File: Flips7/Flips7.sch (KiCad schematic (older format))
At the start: 11 parts, among them U1 FP2800A, U2 FP2800A, U3 FP2800A

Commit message: adding row driver share connectors
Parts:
- added CN1, CN2: Conn_02x16_Odd_Even, Pin_Headers:Pin_Header_Straight_2x16_Pitch2.54mm, symbol Connector_Generic:Conn_02x16_Odd_Even
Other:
- moved on the sheet: BOARD1

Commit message: rename row pins to /SY## and RY##
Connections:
- net labels added: RY01, RY02, RY03, RY04, RY05, RY06, RY07, RY08, RY09, RY10, RY11, RY12, RY13, RY14, RY15, RY16, ~SY01, ~SY02, ~SY03, ~SY04, ~SY05, ~SY06, ~SY07, ~SY08, ~SY09, ~SY10, ~SY11, ~SY12, ~SY13, ~SY14, ~SY15, ~SY16
- net labels removed: YR01, YR02, YR03, YR04, YR05, YR06, YR07, YR08, YR09, YR10, YR11, YR12, YR13, YR14, YR15, YR16, YS01, YS02, YS03, YS04, YS05, YS06, YS07, YS08, YS09, YS10, YS11, YS12, YS13, YS14, YS15, YS16

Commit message: new routing attempt (wip) for Flips7
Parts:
- removed CN1, CN2: Conn_02x16_Odd_Even, Pin_Headers:Pin_Header_Straight_2x16_Pitch2.54mm, symbol Connector_Generic:Conn_02x16_Odd_Even
- added CN1, CN2: Conn_02x17_Odd_Even, Own:Pin_Header_Straight_Shrouded_2x17_Pitch2.54mm_ConvNumbering, symbol Connector_Generic:Conn_02x17_Odd_Even
- BOARD1: footprint IDC_Numbering_Pin_Header_Straight_2x30_Pitch2.54mm -> Own:Pin_Header_Straight_Shrouded_2x30_Pitch2.54mm_AltNumbering
- CNX1, CNY1, CNY2: footprint Own:Pin_Header_Angle_Shrouded_2x05_Pitch2.54mm -> Own:Pin_Header_Angle_Shrouded_2x05_Pitch2.54mm_ConvNumbering
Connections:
- no-connect marks 27 -> 31
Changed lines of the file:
@@
 F 0 "CNY1" H 5150 1517 50  0000 C CNN
 F 1 "UFP2810" H 5150 1426 50  0000 C CNN
-F 2 "Own:Pin_Header_Angle_Shrouded_2x05_Pitch2.54mm" H 5150 1050 50  0001 C CNN
+F 2 "Own:Pin_Header_Angle_Shrouded_2x05_Pitch2.54mm_ConvNumbering" H 5150 1050 50  0001 C CNN
 F 3 "" H 5150 1050 50  0001 C CNN
 	1    5150 1050
@@
 F 0 "CNY2" H 8200 1517 50  0000 C CNN
 F 1 "UFP2810" H 8200 1426 50  0000 C CNN
-F 2 "Own:Pin_Header_Angle_Shrouded_2x05_Pitch2.54mm" H 8200 1050 50  0001 C CNN
+F 2 "Own:Pin_Header_Angle_Shrouded_2x05_Pitch2.54mm_ConvNumbering" H 8200 1050 50  0001 C CNN
 F 3 "" H 8200 1050 50  0001 C CNN
 	1    8200 1050
@@
 F 0 "CNX1" H 2250 5667 50  0000 C CNN
 F 1 "UFP2810" H 2250 5576 50  0000 C CNN
-F 2 "Own:Pin_Header_Angle_Shrouded_2x05_Pitch2.54mm" H 2250 5200 50  0001 C CNN
+F 2 "Own:Pin_Header_Angle_Shrouded_2x05_Pitch2.54mm_ConvNumbering" H 2250 5200 50  0001 C CNN
 F 3 "" H 2250 5200 50  0001 C CNN
 	1    2250 5200
@@
 F 0 "BOARD1" H 6050 5817 50  0000 C CNN
 F 1 "Conn_02x30_Top_Bottom" H 6050 5726 50  0000 C CNN
-F 2 "IDC_Numbering_Pin_Header_Straight_2x30_Pitch2.54mm" H 6000 4200 50  0001 C CNN
+F 2 "Own:Pin_Header_Straight_Shrouded_2x30_Pitch2.54mm_AltNumbering" H 6000 4200 50  0001 C CNN
 F 3 "~" H 6000 4200 50  0001 C CNN
 	1    6000 4200
@@
 Text Label 8300 4400 2    50   ~ 0
 ~SY04
+Text Label 8300 4600 2    50   ~ 0
+~SY05
 Text Label 8300 4500 2    50   ~ 0
-~SY05
-Text Label 8300 4600 2    50   ~ 0
 ~SY06
 Text Label 8300 4700 2    50   ~ 0
 ~SY07
+Text Label 8300 5100 2    50   ~ 0
+~SY08
+Text Label 8300 5200 2    50   ~ 0
+~SY09
+Text Label 8300 5300 2    50   ~ 0
+~SY10
+Text Label 8300 5500 2    50   ~ 0
+~SY11
+Text Label 8300 4900 2    50   ~ 0
+~SY12
+Text Label 8300 5400 2    50   ~ 0
+~SY13
 Text Label 8300 4800 2    50   ~ 0
-~SY08
-Text Label 8300 4900 2    50   ~ 0
-~SY09
-Text Label 8300 5000 2    50   ~ 0
-~SY10
-Text Label 8300 5100 2    50   ~ 0
-~SY11
-Text Label 8300 5200 2    50   ~ 0
-~SY12
-Text Label 8300 5300 2    50   ~ 0
-~SY13
-Text Label 8300 5400 2    50   ~ 0
 ~SY14
-Text Label 8800 4100 0    50   ~ 0
+Text Label 10000 5100 0    50   ~ 0
 RY01
-Text Label 8800 4200 0    50   ~ 0
+Text Label 10000 5200 0    50   ~ 0
 RY02
-Text Label 8800 4300 0    50   ~ 0
+Text Label 10000 5300 0    50   ~ 0
 RY03
-Text Label 8800 4400 0    50   ~ 0
+Text Label 8800 5500 0    50   ~ 0
 RY04
-Text Label 8800 4500 0    50   ~ 0
+Text Label 8800 4900 0    50   ~ 0
 RY05
+Text Label 8800 5400 0    50   ~ 0
+RY06
+Text Label 10000 4800 0    50   ~ 0
+RY07
+Text Label 10000 4100 0    50   ~ 0
+RY08
+Text Label 10000 4200 0    50   ~ 0
+RY09
+Text Label 10000 4300 0    50   ~ 0
+RY10
+Text Label 10000 4400 0    50   ~ 0
+RY11
 Text Label 8800 4600 0    50   ~ 0
-RY06
-Text Label 8800 4700 0    50   ~ 0
-RY07
-Text Label 8800 4800 0    50   ~ 0
-RY08
-Text Label 8800 4900 0    50   ~ 0
-RY09
-Text Label 8800 5000 0    50   ~ 0
-RY10
-Text Label 8800 5100 0    50   ~ 0
-RY11
-Text Label 8800 5200 0    50   ~ 0
 RY12
-Text Label 8800 5300 0    50   ~ 0
+Text Label 10000 4500 0    50   ~ 0
 RY13
-Text Label 8800 5400 0    50   ~ 0
+Text Label 10000 4700 0    50   ~ 0
 RY14
-Text Label 8300 5500 2    50   ~ 0
+Text Label 8300 5600 2    50   ~ 0
 ~SY15
-Text Label 8300 5600 2    50   ~ 0
+Text Label 8300 5700 2    50   ~ 0
 ~SY16
-Text Label 8800 5500 0    50   ~ 0
+Text Label 10000 5600 0    50   ~ 0
 RY15
-Text Label 8800 5600 0    50   ~ 0
+Text Label 10000 5700 0    50   ~ 0
 RY16
 Text Label 9500 4100 2    50   ~ 0
@@
 Text Label 9500 4400 2    50   ~ 0
 ~SY04
+Text Label 9500 4600 2    50   ~ 0
+~SY05
 Text Label 9500 4500 2    50   ~ 0
-~SY05
-Text Label 9500 4600 2    50   ~ 0
 ~SY06
 Text Label 9500 4700 2    50   ~ 0
 ~SY07
+Text Label 9500 5100 2    50   ~ 0
+~SY08
+Text Label 9500 5200 2    50   ~ 0
+~SY09
+Text Label 9500 5300 2    50   ~ 0
+~SY10
+Text Label 9500 5500 2    50   ~ 0
+~SY11
+Text Label 9500 4900 2    50   ~ 0
+~SY12
+Text Label 9500 5400 2    50   ~ 0
+~SY13
 Text Label 9500 4800 2    50   ~ 0
-~SY08
-Text Label 9500 4900 2    50   ~ 0
-~SY09
-Text Label 9500 5000 2    50   ~ 0
-~SY10
-Text Label 9500 5100 2    50   ~ 0
-~SY11
-Text Label 9500 5200 2    50   ~ 0
-~SY12
-Text Label 9500 5300 2    50   ~ 0
-~SY13
-Text Label 9500 5400 2    50   ~ 0
 ~SY14
-Text Label 10000 4100 0    50   ~ 0
+Text Label 8800 5100 0    50   ~ 0
 RY01
-Text Label 10000 4200 0    50   ~ 0
+Text Label 8800 5200 0    50   ~ 0
 RY02
-Text Label 10000 4300 0    50   ~ 0
+Text Label 8800 5300 0    50   ~ 0
 RY03
-Text Label 10000 4400 0    50   ~ 0
+Text Label 10000 5500 0    50   ~ 0
 RY04
-Text Label 10000 4500 0    50   ~ 0
+Text Label 10000 4900 0    50   ~ 0
 RY05
+Text Label 10000 5400 0    50   ~ 0
+RY06
+Text Label 8800 4800 0    50   ~ 0
+RY07
+Text Label 8800 4100 0    50   ~ 0
+RY08
+Text Label 8800 4200 0    50   ~ 0
+RY09
+Text Label 8800 4300 0    50   ~ 0
+RY10
+Text Label 8800 4400 0    50   ~ 0
+RY11
 Text Label 10000 4600 0    50   ~ 0
-RY06
-Text Label 10000 4700 0    50   ~ 0
-RY07
-Text Label 10000 4800 0    50   ~ 0
-RY08
-Text Label 10000 4900 0    50   ~ 0
-RY09
-Text Label 10000 5000 0    50   ~ 0
-RY10
-Text Label 10000 5100 0    50   ~ 0
-RY11
-Text Label 10000 5200 0    50   ~ 0
 RY12
-Text Label 10000 5300 0    50   ~ 0
+Text Label 8800 4500 0    50   ~ 0
 RY13
-Text Label 10000 5400 0    50   ~ 0
+Text Label 8800 4700 0    50   ~ 0
 RY14
-Text Label 9500 5500 2    50   ~ 0
+Text Label 9500 5600 2    50   ~ 0
 ~SY15
-Text Label 9500 5600 2    50   ~ 0
+Text Label 9500 5700 2    50   ~ 0
 ~SY16
-Text Label 10000 5500 0    50   ~ 0
+Text Label 8800 5600 0    50   ~ 0
 RY15
-Text Label 10000 5600 0    50   ~ 0
+Text Label 8800 5700 0    50   ~ 0
 RY16
 $Comp
-L Connector_Generic:Conn_02x16_Odd_Even CN1
-U 1 1 5BE0CD77
-P 8500 4800
-F 0 "CN1" H 8550 5717 50  0000 C CNN
-F 1 "Conn_02x16_Odd_Even" H 8550 5626 50  0000 C CNN
-F 2 "Pin_Headers:Pin_Header_Straight_2x16_Pitch2.54mm" H 8500 4800 50  0001 C CNN
-F 3 "~" H 8500 4800 50  0001 C CNN
-	1    8500 4800
+L Connector_Generic:Conn_02x17_Odd_Even CN1
+U 1 1 5BEB5E2C
+P 8500 4900
+F 0 "CN1" H 8550 5917 50  0000 C CNN
+F 1 "Conn_02x17_Odd_Even" H 8550 5826 50  0000 C CNN
+F 2 "Own:Pin_Header_Straight_Shrouded_2x17_Pitch2.54mm_ConvNumbering" H 8500 4900 50  0001 C CNN
+F 3 "~" H 8500 4900 50  0001 C CNN
+	1    8500 4900
 	1    0    0    -1
 $EndComp
 $Comp
-L Connector_Generic:Conn_02x16_Odd_Even CN2
-U 1 1 5BE0CDEE
-P 9700 4800
-F 0 "CN2" H 9750 5717 50  0000 C CNN
-F 1 "Conn_02x16_Odd_Even" H 9750 5626 50  0000 C CNN
-F 2 "Pin_Headers:Pin_Header_Straight_2x16_Pitch2.54mm" H 9700 4800 50  0001 C CNN
-F 3 "~" H 9700 4800 50  0001 C CNN
-	1    9700 4800
+L Connector_Generic:Conn_02x17_Odd_Even CN2
+U 1 1 5BEB679A
+P 9700 4900
+F 0 "CN2" H 9750 5917 50  0000 C CNN
+F 1 "Conn_02x17_Odd_Even" H 9750 5826 50  0000 C CNN
+F 2 "Own:Pin_Header_Straight_Shrouded_2x17_Pitch2.54mm_ConvNumbering" H 9700 4900 50  0001 C CNN
+F 3 "~" H 9700 4900 50  0001 C CNN
+	1    9700 4900
 	1    0    0    -1
 $EndComp
+NoConn ~ 8300 5000
+NoConn ~ 8800 5000
+NoConn ~ 9500 5000
+NoConn ~ 10000 5000
 $EndSCHEMATC

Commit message: single GND, VCC and HV; almost finish tracing
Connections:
- net labels added: GND, HV, VCC
- net labels removed: L.GND, L.HV, L.VCC, R.GND, R.HV, R.VCC, X.GND, X.HV, X.VCC
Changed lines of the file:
@@
 L.EN
 Text Label 4800 1050 2    50   ~ 0
-L.HV
+HV
 Text Label 4800 1150 2    50   ~ 0
-L.VCC
+VCC
 Text Label 4800 1250 2    50   ~ 0
 L.A0
@@
 L.POL
 Text Label 5500 1050 0    50   ~ 0
-L.GND
+GND
 Text Label 5500 1150 0    50   ~ 0
 L.A1
@@
 R.A0
 Text Label 600  2000 1    50   ~ 0
-L.GND
+GND
 Text Label 600  2450 1    50   ~ 0
-L.GND
+GND
 Text Label 4600 1950 0    50   ~ 0
-L.VCC
+VCC
 Text Label 4600 2350 0    50   ~ 0
-L.HV
+HV
 Text Label 8550 850  0    50   ~ 0
 R.B0
@@
 R.POL
 Text Label 8550 1050 0    50   ~ 0
-R.GND
+GND
 Text Label 8550 1150 0    50   ~ 0
 R.A1
@@
 R.EN
 Text Label 7850 1050 2    50   ~ 0
-R.HV
+HV
 Text Label 7850 1150 2    50   ~ 0
-R.VCC
+VCC
 Text Label 7850 1250 2    50   ~ 0
 R.A0
 Text Label 6750 2100 2    50   ~ 0
-R.GND
+GND
 Text Label 6750 2550 2    50   ~ 0
-R.GND
+GND
 Text Label 10750 2450 0    50   ~ 0
-R.HV
+HV
 Text Label 10750 2050 0    50   ~ 0
-R.VCC
+VCC
 $Comp
 L power:PWR_FLAG #FLG0101
@@
 	0    -1   -1   0
 $EndComp
-$Comp
-L power:PWR_FLAG #FLG0104
-U 1 1 5BDFAC70
-P 2450 750
-F 0 "#FLG0104" H 2450 825 50  0001 C CNN
-F 1 "PWR_FLAG" V 2450 878 50  0000 L CNN
-F 2 "" H 2450 750 50  0001 C CNN
-F 3 "~" H 2450 750 50  0001 C CNN
-	1    2450 750
-	0    -1   -1   0
-$EndComp
-$Comp
-L power:PWR_FLAG #FLG0105
-U 1 1 5BDFAC85
-P 2450 850
-F 0 "#FLG0105" H 2450 925 50  0001 C CNN
-F 1 "PWR_FLAG" V 2450 978 50  0000 L CNN
-F 2 "" H 2450 850 50  0001 C CNN
-F 3 "~" H 2450 850 50  0001 C CNN
-	1    2450 850
-	0    -1   -1   0
-$EndComp
-$Comp
-L power:PWR_FLAG #FLG0106
-U 1 1 5BDFAC9A
-P 2450 950
-F 0 "#FLG0106" H 2450 1025 50  0001 C CNN
-F 1 "PWR_FLAG" V 2450 1078 50  0000 L CNN
-F 2 "" H 2450 950 50  0001 C CNN
-F 3 "~" H 2450 950 50  0001 C CNN
-	1    2450 950
-	0    -1   -1   0
-$EndComp
 Text Label 1500 750  0    50   ~ 0
-L.GND
+GND
 Text Label 1500 850  0    50   ~ 0
-L.VCC
+VCC
 Text Label 1500 950  0    50   ~ 0
-L.HV
-Text Label 2450 750  0    50   ~ 0
-R.GND
-Text Label 2450 850  0    50   ~ 0
-R.VCC
-Text Label 2450 950  0    50   ~ 0
-R.HV
+HV
 $Comp
 L Device:C_Small C1
@@
 	4600 1600 4600 1650
 Text Label 4600 1600 0    50   ~ 0
-L.GND
+GND
 Text Label 10750 1700 0    50   ~ 0
-R.GND
+GND
 Text Label 4050 3050 3    50   ~ 0
 ~SY01
@@
 X.POL
 Text Label 2600 5200 0    50   ~ 0
-X.GND
+GND
 Text Label 2600 5300 0    50   ~ 0
 X.A1
@@
 X.EN
 Text Label 1900 5200 2    50   ~ 0
-X.HV
+HV
 Text Label 1900 5300 2    50   ~ 0
-X.VCC
+VCC
 Text Label 1900 5400 2    50   ~ 0
 X.A0
 Text Label 800  6250 2    50   ~ 0
-X.GND
+GND
 Text Label 800  6700 2    50   ~ 0
-X.GND
+GND
 Text Label 4800 6600 0    50   ~ 0
-X.HV
+HV
 Text Label 4800 6200 0    50   ~ 0
-X.VCC
+VCC
 $Comp
 L Device:C_Small C3
@@
 	4800 6100 4800 6200
 Text Label 4800 5850 0    50   ~ 0
-X.GND
+GND
 Text Label 4250 7300 3    50   ~ 0
 X01
@@
 NoConn ~ 4450 7300
 $Comp
-L power:PWR_FLAG #FLG01
-U 1 1 5BE4CDC2
-P 3400 750
-F 0 "#FLG01" H 3400 825 50  0001 C CNN
-F 1 "PWR_FLAG" V 3400 878 50  0000 L CNN
-F 2 "" H 3400 750 50  0001 C CNN
-F 3 "~" H 3400 750 50  0001 C CNN
-	1    3400 750
-	0    -1   -1   0
-$EndComp
-$Comp
-L power:PWR_FLAG #FLG02
-U 1 1 5BE4CDC8
-P 3400 850
-F 0 "#FLG02" H 3400 925 50  0001 C CNN
-F 1 "PWR_FLAG" V 3400 978 50  0000 L CNN
-F 2 "" H 3400 850 50  0001 C CNN
-F 3 "~" H 3400 850 50  0001 C CNN
-	1    3400 850
-	0    -1   -1   0
-$EndComp
-$Comp
-L power:PWR_FLAG #FLG03
-U 1 1 5BE4CDCE
-P 3400 950
-F 0 "#FLG03" H 3400 1025 50  0001 C CNN
-F 1 "PWR_FLAG" V 3400 1078 50  0000 L CNN
-F 2 "" H 3400 950 50  0001 C CNN
-F 3 "~" H 3400 950 50  0001 C CNN
-	1    3400 950
-	0    -1   -1   0
-$EndComp
-Text Label 3400 750  0    50   ~ 0
-X.GND
-Text Label 3400 850  0    50   ~ 0
-X.VCC
-Text Label 3400 950  0    50   ~ 0
-X.HV
-$Comp
 L Connector_Generic:Conn_02x30_Top_Bottom BOARD1

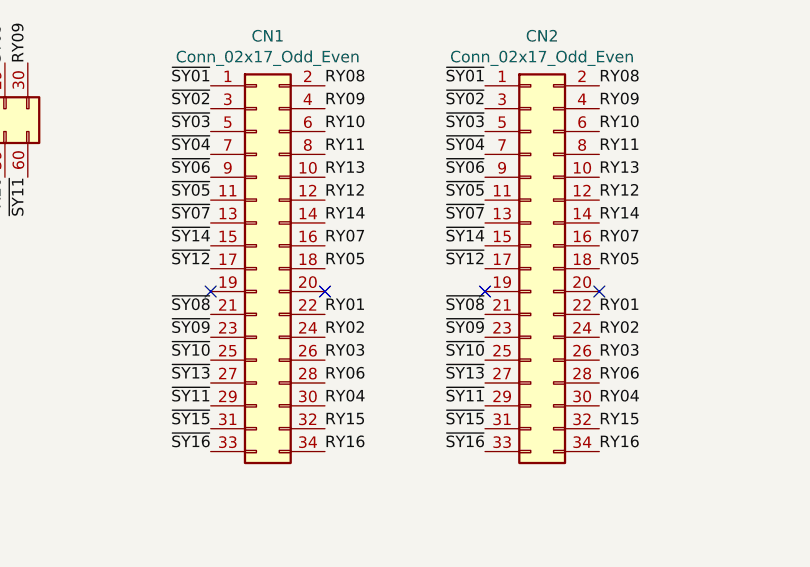
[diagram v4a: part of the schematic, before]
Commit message: GND on share connectors
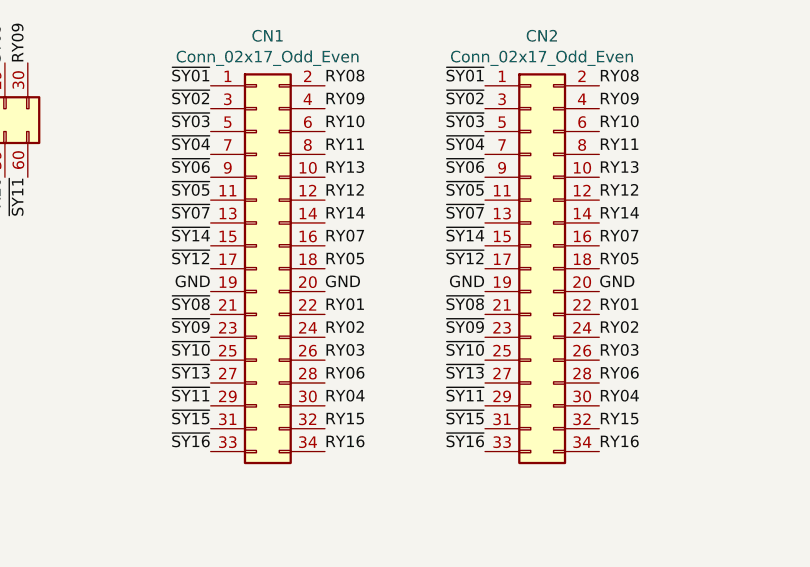
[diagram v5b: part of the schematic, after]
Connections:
- no-connect marks 31 -> 27
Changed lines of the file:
@@
 	1    0    0    -1
 $EndComp
-NoConn ~ 8300 5000
-NoConn ~ 8800 5000
-NoConn ~ 9500 5000
-NoConn ~ 10000 5000
+Text Label 8300 5000 2    50   ~ 0
+GND
+Text Label 9500 5000 2    50   ~ 0
+GND
+Text Label 8800 5000 0    50   ~ 0
+GND
+Text Label 10000 5000 0    50   ~ 0
+GND
 $EndSCHEMATC

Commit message: Fixing C values to 0µ1; connecting VCC of 3 units
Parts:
- C1, C2, C3: value 0U1 -> 0µ1
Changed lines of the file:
@@
 P 4600 1750
 F 0 "C1" H 4692 1796 50  0000 L CNN
-F 1 "0U1" H 4692 1705 50  0000 L CNN
+F 1 "0µ1" H 4692 1705 50  0000 L CNN
 F 2 "Capacitors_SMD:C_0805_HandSoldering" H 4600 1750 50  0001 C CNN
 F 3 "~" H 4600 1750 50  0001 C CNN
@@
 P 10750 1850
 F 0 "C2" H 10658 1804 50  0000 R CNN
-F 1 "0U1" H 10658 1895 50  0000 R CNN
+F 1 "0µ1" H 10658 1895 50  0000 R CNN
 F 2 "Capacitors_SMD:C_0805_HandSoldering" H 10750 1850 50  0001 C CNN
 F 3 "~" H 10750 1850 50  0001 C CNN
@@
 P 4800 6000
 F 0 "C3" H 4708 5954 50  0000 R CNN
-F 1 "0U1" H 4708 6045 50  0000 R CNN
+F 1 "0µ1" H 4708 6045 50  0000 R CNN
 F 2 "Capacitors_SMD:C_0805_HandSoldering" H 4800 6000 50  0001 C CNN
 F 3 "~" H 4800 6000 50  0001 C CNN

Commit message: adding pull downs for ENABLE pins
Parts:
- added R1, R2, R3: 10k, Resistors_SMD:R_0805_HandSoldering, symbol Device:R_Small
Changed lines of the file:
@@
 Text Label 10000 5000 0    50   ~ 0
 GND
+$Comp
+L Device:R_Small R3
+U 1 1 5BEF1C78
+P 1350 4150
+F 0 "R3" H 1409 4196 50  0000 L CNN
+F 1 "10k" H 1409 4105 50  0000 L CNN
+F 2 "Resistors_SMD:R_0805_HandSoldering" H 1350 4150 50  0001 C CNN
+F 3 "~" H 1350 4150 50  0001 C CNN
+	1    1350 4150
+	1    0    0    -1
+$EndComp
+$Comp
+L power:GND #PWR0101
+U 1 1 5BEF1DC6
+P 1350 4250
+F 0 "#PWR0101" H 1350 4000 50  0001 C CNN
+F 1 "GND" H 1355 4077 50  0000 C CNN
+F 2 "" H 1350 4250 50  0001 C CNN
+F 3 "" H 1350 4250 50  0001 C CNN
+	1    1350 4250
+	1    0    0    -1
+$EndComp
+Text Label 1350 4050 0    50   ~ 0
+X.EN
+$Comp
+L Device:R_Small R1
+U 1 1 5BEF1F26
+P 2600 1000
+F 0 "R1" H 2659 1046 50  0000 L CNN
+F 1 "10k" H 2659 955 50  0000 L CNN
+F 2 "Resistors_SMD:R_0805_HandSoldering" H 2600 1000 50  0001 C CNN
+F 3 "~" H 2600 1000 50  0001 C CNN
+	1    2600 1000
+	1    0    0    -1
+$EndComp
+$Comp
+L power:GND #PWR0102
+U 1 1 5BEF1F2D
+P 2600 1100
+F 0 "#PWR0102" H 2600 850 50  0001 C CNN
+F 1 "GND" H 2605 927 50  0000 C CNN
+F 2 "" H 2600 1100 50  0001 C CNN
+F 3 "" H 2600 1100 50  0001 C CNN
+	1    2600 1100
+	1    0    0    -1
+$EndComp
+Text Label 2600 900  0    50   ~ 0
+L.EN
+$Comp
+L Device:R_Small R2
+U 1 1 5BEF202A
+P 10450 1000
+F 0 "R2" H 10509 1046 50  0000 L CNN
+F 1 "10k" H 10509 955 50  0000 L CNN
+F 2 "Resistors_SMD:R_0805_HandSoldering" H 10450 1000 50  0001 C CNN
+F 3 "~" H 10450 1000 50  0001 C CNN
+	1    10450 1000
+	1    0    0    -1
+$EndComp
+$Comp
+L power:GND #PWR0103
+U 1 1 5BEF2031
+P 10450 1100
+F 0 "#PWR0103" H 10450 850 50  0001 C CNN
+F 1 "GND" H 10455 927 50  0000 C CNN
+F 2 "" H 10450 1100 50  0001 C CNN
+F 3 "" H 10450 1100 50  0001 C CNN
+	1    10450 1100
+	1    0    0    -1
+$EndComp
+Text Label 10450 900  0    50   ~ 0
+R.EN
 $EndSCHEMATC

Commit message: rename some symbols
rename L.## and R.## nets to Y1.## and Y2.##
rename CN1 and CN2 to SHR1 and SHR2
rename U1/2/3 to IC1/2/3
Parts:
- renumbered U1 to IC1, U2 to IC2, U3 to IC3, CN1 to SHR1, CN2 to SHR2
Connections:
- net labels added: Y1.A0, Y1.A1, Y1.A2, Y1.B0, Y1.B1, Y1.EN, Y1.POL, Y2.A0, Y2.A1, Y2.A2, Y2.B0, Y2.B1, Y2.EN, Y2.POL
- net labels removed: L.A0, L.A1, L.A2, L.B0, L.B1, L.EN, L.POL, R.A0, R.A1, R.A2, R.B0, R.B1, R.EN, R.POL
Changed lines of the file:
@@
 $EndDescr
 $Comp
-L Eigene~Bauteile:FP2800A U1
+L Eigene~Bauteile:FP2800A IC1
 U 1 1 5B82C6BE
 P 2350 2250
-F 0 "U1" V 2200 4500 60  0000 L CNN
+F 0 "IC1" V 2200 4500 60  0000 L CNN
 F 1 "FP2800A" V 2300 4500 60  0000 L CNN
 F 2 "Housings_DIP:DIP-40_W15.24mm_Socket" H 2300 2350 60  0001 C CNN
@@
 $EndComp
 $Comp
-L Eigene~Bauteile:FP2800A U2
+L Eigene~Bauteile:FP2800A IC2
 U 1 1 5B82C7AE
 P 8500 2350
-F 0 "U2" V 8350 4650 60  0000 L CNN
+F 0 "IC2" V 8350 4650 60  0000 L CNN
 F 1 "FP2800A" V 8450 4650 60  0000 L CNN
 F 2 "Housings_DIP:DIP-40_W15.24mm_Socket" H 8450 2450 60  0001 C CNN
@@
 $EndComp
 Text Label 4800 850  2    50   ~ 0
-L.B1
+Y1.B1
 Text Label 4800 950  2    50   ~ 0
-L.EN
+Y1.EN
 Text Label 4800 1050 2    50   ~ 0
 HV
@@
 VCC
 Text Label 4800 1250 2    50   ~ 0
-L.A0
+Y1.A0
 Text Label 5500 850  0    50   ~ 0
-L.B0
+Y1.B0
 Text Label 5500 950  0    50   ~ 0
-L.POL
+Y1.POL
 Text Label 5500 1050 0    50   ~ 0
 GND
 Text Label 5500 1150 0    50   ~ 0
-L.A1
+Y1.A1
 Text Label 5500 1250 0    50   ~ 0
-L.A2
+Y1.A2
 Text Label 3050 1400 1    50   ~ 0
-L.EN
+Y1.EN
 Text Label 3250 1400 1    50   ~ 0
-L.POL
+Y1.POL
 Text Label 3450 1400 1    50   ~ 0
-L.B1
+Y1.B1
 Text Label 3550 1400 1    50   ~ 0
-L.B0
+Y1.B0
 Text Label 3750 1400 1    50   ~ 0
-L.A2
+Y1.A2
 Text Label 3850 1400 1    50   ~ 0
-L.A1
+Y1.A1
 Text Label 3950 1400 1    50   ~ 0
-L.A0
+Y1.A0
 Text Label 9200 1500 1    50   ~ 0
-R.EN
+Y2.EN
 Text Label 9400 1500 1    50   ~ 0
-R.POL
+Y2.POL
 Text Label 9600 1500 1    50   ~ 0
-R.B1
+Y2.B1
 Text Label 9700 1500 1    50   ~ 0
-R.B0
+Y2.B0
 Text Label 9900 1500 1    50   ~ 0
-R.A2
+Y2.A2
 Text Label 10000 1500 1    50   ~ 0
-R.A1
+Y2.A1
 Text Label 10100 1500 1    50   ~ 0
-R.A0
+Y2.A0
 Text Label 600  2000 1    50   ~ 0
 GND
@@
 HV
 Text Label 8550 850  0    50   ~ 0
-R.B0
+Y2.B0
 Text Label 8550 950  0    50   ~ 0
-R.POL
+Y2.POL
 Text Label 8550 1050 0    50   ~ 0
 GND
 Text Label 8550 1150 0    50   ~ 0
-R.A1
+Y2.A1
 Text Label 8550 1250 0    50   ~ 0
-R.A2
+Y2.A2
 Text Label 7850 850  2    50   ~ 0
-R.B1
+Y2.B1
 Text Label 7850 950  2    50   ~ 0
-R.EN
+Y2.EN
 Text Label 7850 1050 2    50   ~ 0
 HV
@@
 VCC
 Text Label 7850 1250 2    50   ~ 0
-R.A0
+Y2.A0
 Text Label 6750 2100 2    50   ~ 0
 GND
@@
 $EndComp
 $Comp
-L Eigene~Bauteile:FP2800A U3
+L Eigene~Bauteile:FP2800A IC3
 U 1 1 5BE4BE29
 P 2550 6500
-F 0 "U3" V 2400 8800 60  0000 L CNN
+F 0 "IC3" V 2400 8800 60  0000 L CNN
 F 1 "FP2800A" V 2500 8800 60  0000 L CNN
 F 2 "Housings_DIP:DIP-40_W15.24mm_Socket" H 2500 6600 60  0001 C CNN
@@
 RY16
 $Comp
-L Connector_Generic:Conn_02x17_Odd_Even CN1
+L Connector_Generic:Conn_02x17_Odd_Even SHR1
 U 1 1 5BEB5E2C
 P 8500 4900
-F 0 "CN1" H 8550 5917 50  0000 C CNN
+F 0 "SHR1" H 8550 5917 50  0000 C CNN
 F 1 "Conn_02x17_Odd_Even" H 8550 5826 50  0000 C CNN
 F 2 "Own:Pin_Header_Straight_Shrouded_2x17_Pitch2.54mm_ConvNumbering" H 8500 4900 50  0001 C CNN
@@
 $EndComp
 $Comp
-L Connector_Generic:Conn_02x17_Odd_Even CN2
+L Connector_Generic:Conn_02x17_Odd_Even SHR2
 U 1 1 5BEB679A
 P 9700 4900
-F 0 "CN2" H 9750 5917 50  0000 C CNN
+F 0 "SHR2" H 9750 5917 50  0000 C CNN
 F 1 "Conn_02x17_Odd_Even" H 9750 5826 50  0000 C CNN
 F 2 "Own:Pin_Header_Straight_Shrouded_2x17_Pitch2.54mm_ConvNumbering" H 9700 4900 50  0001 C CNN
@@
 $EndComp
 Text Label 2600 900  0    50   ~ 0
-L.EN
+Y1.EN
 $Comp
 L Device:R_Small R2
@@
 $EndComp
 Text Label 10450 900  0    50   ~ 0
-R.EN
+Y2.EN
 $EndSCHEMATC
